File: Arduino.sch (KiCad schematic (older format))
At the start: 0 parts

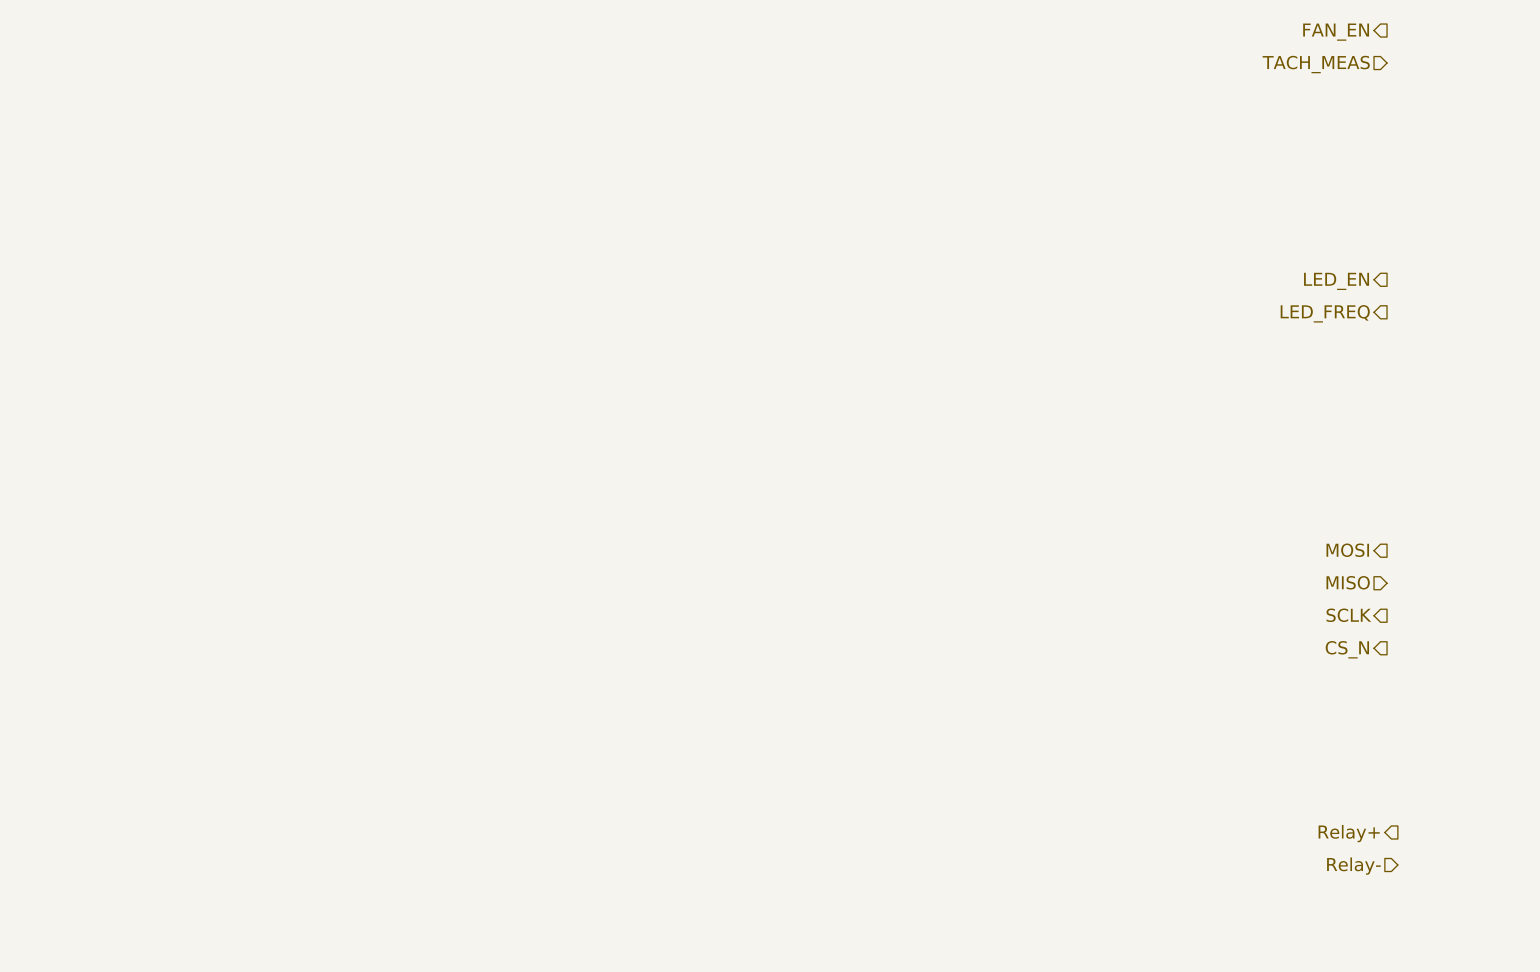
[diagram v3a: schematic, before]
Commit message: Completed Arduino Module Video
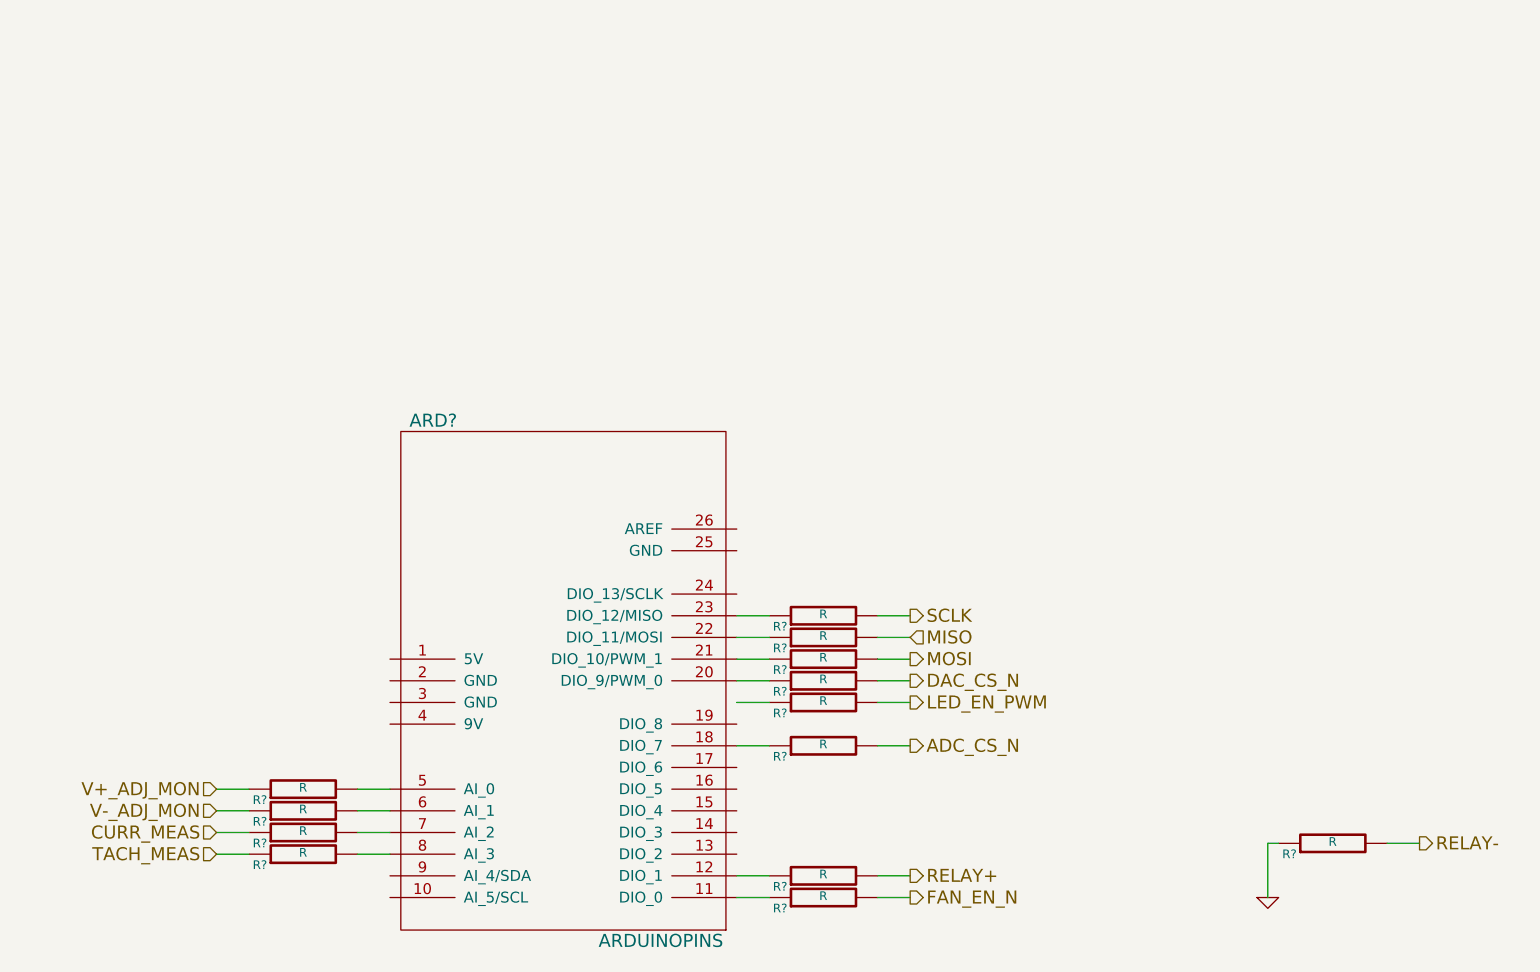
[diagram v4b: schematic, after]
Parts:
- added ARD?: ARDUINOPINS, symbol ARDUINOPINS
- added R? (x13): R, ~, symbol R
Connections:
- net MISO: now also R?.2
- net MOSI: now also R?.2
- net SCLK: now also R?.2
- net TACH_MEAS: now also R?.1
- new net: ARD?.11 (DIO_0), R?.1
- new net: ARD?.12 (DIO_1), R?.1
- new net: ARD?.18 (DIO_7), R?.1
- new net: ARD?.20 (DIO_9/PWM_0), R?.1
- new net: ARD?.21 (DIO_10/PWM_1), R?.1
- new net: ARD?.22 (DIO_11/MOSI), R?.1
- new net: ARD?.23 (DIO_12/MISO), R?.1
- new net: ARD?.5 (AI_0), R?.2
- new net: ARD?.6 (AI_1), R?.2
- new net: ARD?.7 (AI_2), R?.2
- new net: ARD?.8 (AI_3), R?.2
- new net ADC_CS_N: R?.2
- new net CURR_MEAS: R?.1
- new net DAC_CS_N: R?.2
- new net FAN_EN_N: R?.2
- new net GND: R?.1
- new net LED_EN_PWM: R?.2
- new net RELAY+: R?.2
- new net RELAY-: R?.2
- new net V+_ADJ_MON: R?.1
- new net V-_ADJ_MON: R?.1

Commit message: Fan Module Update
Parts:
- removed ARD?: ARDUINOPINS, symbol ARDUINOPINS
- added ARD?: ARDUINOPINS, ~, symbol ARDUINOPINS
- added R? (x2): R, ~, symbol R
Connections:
- net at R?.1: now also ARD?.20 (DIO_9/PWM_0)
- net at R?.1: now also ARD?.12 (DIO_1)
- net at R?.1: now also ARD?.18 (DIO_7)
- net at R?.1: now also ARD?.17 (DIO_6)
- net at R?.1: now also ARD?.21 (DIO_10/PWM_1)
- net at R?.1: now also ARD?.22 (DIO_11/MOSI)
- net at R?.1: now also ARD?.23 (DIO_12/MISO)
- net at R?.2: now also ARD?.5 (AI_0)
- net at R?.2: now also ARD?.6 (AI_1)
- net at R?.2: now also ARD?.7 (AI_2)
- net at R?.2: now also ARD?.8 (AI_3)
- net FAN_EN_N renamed FAN_PWM
- new net: ARD?.11 (DIO_0), R?.1
- new net: ARD?.4 (9V), R?.2
- new net +12P: R?.1
- new net FAN_MODE: R?.2
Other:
- moved on the sheet: R?
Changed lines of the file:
@@
 Text HLabel 6400 4100 2    60   Output ~ 0
 SCLK
+Text HLabel 6400 4800 2    60   Output ~ 0
+DAC_CS_N
 Text HLabel 6400 4400 2    60   Output ~ 0
-DAC_CS_N
-Text HLabel 6400 5400 2    60   Output ~ 0
-FAN_EN_N
+FAN_PWM
 Text HLabel 3200 5200 0    60   Input ~ 0
 TACH_MEAS
-$Comp
-L ARDUINOPINS ARD?
-U 1 1 52F9D8E3
-P 6350 4700
-F 0 "ARD?" H 4200 6200 60  0000 C CNN
-F 1 "ARDUINOPINS" H 5250 3800 60  0000 C CNN
-F 2 "" H 6350 4700 60  0000 C CNN
-F 3 "" H 6350 4700 60  0000 C CNN
-	1    6350 4700
-	1    0    0    -1
-$EndComp
 Text HLabel 3200 5100 0    60   Input ~ 0
 CURR_MEAS
@@
 L R R?
 U 1 1 52F9D91F
-P 6000 5400
-F 0 "R?" V 5950 5600 40  0000 C CNN
-F 1 "R" V 6007 5401 40  0000 C CNN
-F 2 "~" V 5930 5400 30  0000 C CNN
-F 3 "~" H 6000 5400 30  0000 C CNN
-	1    6000 5400
-	0    -1   -1   0
-$EndComp
-Wire Wire Line
-	5600 5400 5750 5400
-Wire Wire Line
-	6250 5400 6400 5400
+P 6000 4400
+F 0 "R?" V 5950 4600 40  0000 C CNN
+F 1 "R" V 6007 4401 40  0000 C CNN
+F 2 "~" V 5930 4400 30  0000 C CNN
+F 3 "~" H 6000 4400 30  0000 C CNN
+	1    6000 4400
+	0    -1   -1   0
+$EndComp
 $Comp
 L R R?
@@
 L R R?
 U 1 1 52FA6082
-P 6000 4400
-F 0 "R?" V 5950 4600 40  0000 C CNN
-F 1 "R" V 6007 4401 40  0000 C CNN
-F 2 "~" V 5930 4400 30  0000 C CNN
-F 3 "~" H 6000 4400 30  0000 C CNN
-	1    6000 4400
+P 6000 4800
+F 0 "R?" V 5950 5000 40  0000 C CNN
+F 1 "R" V 6007 4801 40  0000 C CNN
+F 2 "~" V 5930 4800 30  0000 C CNN
+F 3 "~" H 6000 4800 30  0000 C CNN
+	1    6000 4800
 	0    -1   -1   0
 $EndComp
@@
 $EndComp
 Wire Wire Line
-	6250 4400 6400 4400
-Wire Wire Line
 	6250 4300 6400 4300
 Wire Wire Line
@@
 Wire Wire Line
 	6250 4100 6400 4100
-Wire Wire Line
-	5750 4400 5600 4400
 Wire Wire Line
 	5750 4300 5600 4300
@@
 Wire Wire Line
 	6250 4700 6400 4700
+Wire Wire Line
+	5600 4800 5750 4800
+Wire Wire Line
+	6250 4800 6400 4800
+Wire Wire Line
+	6250 4400 6400 4400
+Wire Wire Line
+	5750 4400 5600 4400
+$Comp
+L ARDUINOPINS ARD?
+U 1 1 52FA4C31
+P 6350 4700
+F 0 "ARD?" H 4200 6200 60  0000 C CNN
+F 1 "ARDUINOPINS" H 5250 3800 60  0000 C CNN
+F 2 "~" H 6350 4700 60  0000 C CNN
+F 3 "~" H 6350 4700 60  0000 C CNN
+	1    6350 4700
+	1    0    0    -1
+$EndComp
+Text HLabel 6400 5400 2    60   Output ~ 0
+FAN_MODE
+$Comp
+L R R?
+U 1 1 52FA55B0
+P 6000 5400
+F 0 "R?" V 5950 5600 40  0000 C CNN
+F 1 "R" V 6007 5401 40  0000 C CNN
+F 2 "~" V 5930 5400 30  0000 C CNN
+F 3 "~" H 6000 5400 30  0000 C CNN
+	1    6000 5400
+	0    -1   -1   0
+$EndComp
+Wire Wire Line
+	5600 5400 5750 5400
+Wire Wire Line
+	6250 5400 6400 5400
+$Comp
+L R R?
+U 1 1 52FA5B06
+P 3600 4600
+F 0 "R?" V 3550 4800 40  0000 C CNN
+F 1 "R" V 3607 4601 40  0000 C CNN
+F 2 "~" V 3530 4600 30  0000 C CNN
+F 3 "~" H 3600 4600 30  0000 C CNN
+	1    3600 4600
+	0    -1   -1   0
+$EndComp
+Wire Wire Line
+	3850 4600 4000 4600
+$Comp
+L +12P #PWR?
+U 1 1 52FA5B4B
+P 2800 4500
+F 0 "#PWR?" H 2800 4470 30  0001 C CNN
+F 1 "+12P" H 2800 4600 30  0000 C CNN
+F 2 "" H 2800 4500 60  0000 C CNN
+F 3 "" H 2800 4500 60  0000 C CNN
+	1    2800 4500
+	1    0    0    -1
+$EndComp
+Wire Wire Line
+	2800 4500 2800 4600
+Wire Wire Line
+	2800 4600 3350 4600
 $EndSCHEMATC

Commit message: Started Layout Outline.  Completed other schem videos
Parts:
- removed ARD?: ARDUINOPINS, ~, symbol ARDUINOPINS
- added ARD?: ARDUINOPINS, ~, symbol ARDUINOPINS
- added R? (x3): R, ~, symbol R
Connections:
- net GND: now also R?.1, R?.1
- net at R?.1: now also ARD?.21 (DIO_10/PWM_1)
- net at R?.1: now also ARD?.12 (DIO_1)
- net at R?.2: now also ARD?.8 (AI_3)
- net at R?.2: now also ARD?.7 (AI_2)
- net at R?.1: now also ARD?.11 (DIO_0)
- net at R?.1: now also ARD?.18 (DIO_7)
- net at R?.1: now also ARD?.19 (DIO_8)
- net at R?.1: now also ARD?.22 (DIO_11/MOSI)
- net at R?.1: now also ARD?.23 (DIO_12/MISO)
- net at R?.1: now also ARD?.24 (DIO_13/SCLK)
- net at R?.2: now also ARD?.4 (9V)
- net at R?.2: now also ARD?.5 (AI_0)
- net at R?.2: now also ARD?.6 (AI_1)
- net at R?.1: now also ARD?.20 (DIO_9/PWM_0)
- new net: ARD?.1 (5V), R?.2
- new net: ARD?.2 (GND), R?.2
- new net: ARD?.3 (GND), R?.2
- new net +5V: R?.1
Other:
- moved on the sheet: R?
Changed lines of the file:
@@
 $Descr A4 11693 8268
 encoding utf-8
-Sheet 2 9
+Sheet 9 9
 Title ""
-Date "11 feb 2014"
+Date "17 feb 2014"
 Rev ""
 Comp ""
@@
 Text HLabel 8750 5150 2    60   Output ~ 0
 RELAY-
+Text HLabel 6400 4200 2    60   Output ~ 0
+MOSI
+Text HLabel 6400 4100 2    60   Input ~ 0
+MISO
+Text HLabel 6400 4000 2    60   Output ~ 0
+SCLK
+Text HLabel 6400 4700 2    60   Output ~ 0
+DAC_CS_N
 Text HLabel 6400 4300 2    60   Output ~ 0
-MOSI
-Text HLabel 6400 4200 2    60   Input ~ 0
-MISO
-Text HLabel 6400 4100 2    60   Output ~ 0
-SCLK
-Text HLabel 6400 4800 2    60   Output ~ 0
-DAC_CS_N
-Text HLabel 6400 4400 2    60   Output ~ 0
 FAN_PWM
 Text HLabel 3200 5200 0    60   Input ~ 0
@@
 L R R?
 U 1 1 52F9D91F
-P 6000 4400
-F 0 "R?" V 5950 4600 40  0000 C CNN
-F 1 "R" V 6007 4401 40  0000 C CNN
-F 2 "~" V 5930 4400 30  0000 C CNN
-F 3 "~" H 6000 4400 30  0000 C CNN
-	1    6000 4400
+P 6000 4300
+F 0 "R?" V 5950 4500 40  0000 C CNN
+F 1 "R" V 6007 4301 40  0000 C CNN
+F 2 "~" V 5930 4300 30  0000 C CNN
+F 3 "~" H 6000 4300 30  0000 C CNN
+	1    6000 4300
 	0    -1   -1   0
 $EndComp
@@
 L R R?
 U 1 1 52FA6082
-P 6000 4800
-F 0 "R?" V 5950 5000 40  0000 C CNN
-F 1 "R" V 6007 4801 40  0000 C CNN
-F 2 "~" V 5930 4800 30  0000 C CNN
-F 3 "~" H 6000 4800 30  0000 C CNN
-	1    6000 4800
+P 6000 4700
+F 0 "R?" V 5950 4900 40  0000 C CNN
+F 1 "R" V 6007 4701 40  0000 C CNN
+F 2 "~" V 5930 4700 30  0000 C CNN
+F 3 "~" H 6000 4700 30  0000 C CNN
+	1    6000 4700
 	0    -1   -1   0
 $EndComp
@@
 L R R?
 U 1 1 52FA6088
-P 6000 4300
-F 0 "R?" V 5950 4500 40  0000 C CNN
-F 1 "R" V 6007 4301 40  0000 C CNN
-F 2 "~" V 5930 4300 30  0000 C CNN
-F 3 "~" H 6000 4300 30  0000 C CNN
-	1    6000 4300
-	0    -1   -1   0
-$EndComp
-$Comp
-L R R?
-U 1 1 52FA608E
 P 6000 4200
 F 0 "R?" V 5950 4400 40  0000 C CNN
@@
 $Comp
 L R R?
-U 1 1 52FA6094
+U 1 1 52FA608E
 P 6000 4100
 F 0 "R?" V 5950 4300 40  0000 C CNN
@@
 	0    -1   -1   0
 $EndComp
+$Comp
+L R R?
+U 1 1 52FA6094
+P 6000 4000
+F 0 "R?" V 5950 4200 40  0000 C CNN
+F 1 "R" V 6007 4001 40  0000 C CNN
+F 2 "~" V 5930 4000 30  0000 C CNN
+F 3 "~" H 6000 4000 30  0000 C CNN
+	1    6000 4000
+	0    -1   -1   0
+$EndComp
+Wire Wire Line
+	6250 4200 6400 4200
+Wire Wire Line
+	6250 4100 6400 4100
+Wire Wire Line
+	6250 4000 6400 4000
+Wire Wire Line
+	5750 4200 5600 4200
+Wire Wire Line
+	5750 4100 5600 4100
+Wire Wire Line
+	5750 4000 5600 4000
+Text HLabel 6400 4400 2    60   Output ~ 0
+LED_EN_PWM
+$Comp
+L R R?
+U 1 1 52FA63A1
+P 6000 4400
+F 0 "R?" V 5950 4600 40  0000 C CNN
+F 1 "R" V 6007 4401 40  0000 C CNN
+F 2 "~" V 5930 4400 30  0000 C CNN
+F 3 "~" H 6000 4400 30  0000 C CNN
+	1    6000 4400
+	0    -1   -1   0
+$EndComp
+Wire Wire Line
+	5750 4400 5600 4400
+Wire Wire Line
+	6250 4400 6400 4400
+Text HLabel 6400 4600 2    60   Output ~ 0
+ADC_CS_N
+$Comp
+L R R?
+U 1 1 52FA944C
+P 6000 4600
+F 0 "R?" V 5950 4800 40  0000 C CNN
+F 1 "R" V 6007 4601 40  0000 C CNN
+F 2 "~" V 5930 4600 30  0000 C CNN
+F 3 "~" H 6000 4600 30  0000 C CNN
+	1    6000 4600
+	0    -1   -1   0
+$EndComp
+Wire Wire Line
+	5600 4600 5750 4600
+Wire Wire Line
+	6250 4600 6400 4600
+Wire Wire Line
+	5600 4700 5750 4700
+Wire Wire Line
+	6250 4700 6400 4700
 Wire Wire Line
 	6250 4300 6400 4300
 Wire Wire Line
-	6250 4200 6400 4200
-Wire Wire Line
-	6250 4100 6400 4100
-Wire Wire Line
 	5750 4300 5600 4300
-Wire Wire Line
-	5750 4200 5600 4200
-Wire Wire Line
-	5750 4100 5600 4100
-Text HLabel 6400 4500 2    60   Output ~ 0
-LED_EN_PWM
-$Comp
-L R R?
-U 1 1 52FA63A1
-P 6000 4500
-F 0 "R?" V 5950 4700 40  0000 C CNN
-F 1 "R" V 6007 4501 40  0000 C CNN
-F 2 "~" V 5930 4500 30  0000 C CNN
-F 3 "~" H 6000 4500 30  0000 C CNN
-	1    6000 4500
-	0    -1   -1   0
-$EndComp
-Wire Wire Line
-	5750 4500 5600 4500
-Wire Wire Line
-	6250 4500 6400 4500
-Text HLabel 6400 4700 2    60   Output ~ 0
-ADC_CS_N
-$Comp
-L R R?
-U 1 1 52FA944C
-P 6000 4700
-F 0 "R?" V 5950 4900 40  0000 C CNN
-F 1 "R" V 6007 4701 40  0000 C CNN
-F 2 "~" V 5930 4700 30  0000 C CNN
-F 3 "~" H 6000 4700 30  0000 C CNN
-	1    6000 4700
-	0    -1   -1   0
-$EndComp
-Wire Wire Line
-	5600 4700 5750 4700
-Wire Wire Line
-	6250 4700 6400 4700
-Wire Wire Line
-	5600 4800 5750 4800
-Wire Wire Line
-	6250 4800 6400 4800
-Wire Wire Line
-	6250 4400 6400 4400
-Wire Wire Line
-	5750 4400 5600 4400
-$Comp
-L ARDUINOPINS ARD?
-U 1 1 52FA4C31
-P 6350 4700
-F 0 "ARD?" H 4200 6200 60  0000 C CNN
-F 1 "ARDUINOPINS" H 5250 3800 60  0000 C CNN
-F 2 "~" H 6350 4700 60  0000 C CNN
-F 3 "~" H 6350 4700 60  0000 C CNN
-	1    6350 4700
-	1    0    0    -1
-$EndComp
 Text HLabel 6400 5400 2    60   Output ~ 0
 FAN_MODE
@@
 L +12P #PWR?
 U 1 1 52FA5B4B
-P 2800 4500
-F 0 "#PWR?" H 2800 4470 30  0001 C CNN
-F 1 "+12P" H 2800 4600 30  0000 C CNN
-F 2 "" H 2800 4500 60  0000 C CNN
-F 3 "" H 2800 4500 60  0000 C CNN
-	1    2800 4500
-	1    0    0    -1
-$EndComp
-Wire Wire Line
-	2800 4500 2800 4600
-Wire Wire Line
-	2800 4600 3350 4600
+P 2350 4500
+F 0 "#PWR?" H 2350 4470 30  0001 C CNN
+F 1 "+12P" H 2350 4600 30  0000 C CNN
+F 2 "" H 2350 4500 60  0000 C CNN
+F 3 "" H 2350 4500 60  0000 C CNN
+	1    2350 4500
+	1    0    0    -1
+$EndComp
+Wire Wire Line
+	2350 4500 2350 4650
+$Comp
+L ARDUINOPINS ARD?
+U 1 1 53022634
+P 6350 4700
+F 0 "ARD?" H 4200 6200 60  0000 C CNN
+F 1 "ARDUINOPINS" H 5250 3800 60  0000 C CNN
+F 2 "~" H 6350 4700 60  0000 C CNN
+F 3 "~" H 6350 4700 60  0000 C CNN
+	1    6350 4700
+	1    0    0    -1
+$EndComp
+$Comp
+L R R?
+U 1 1 53023A69
+P 3600 4300
+F 0 "R?" V 3550 4500 40  0000 C CNN
+F 1 "R" V 3607 4301 40  0000 C CNN
+F 2 "~" V 3530 4300 30  0000 C CNN
+F 3 "~" H 3600 4300 30  0000 C CNN
+	1    3600 4300
+	0    -1   -1   0
+$EndComp
+$Comp
+L R R?
+U 1 1 53023A6F
+P 3600 4400
+F 0 "R?" V 3550 4600 40  0000 C CNN
+F 1 "R" V 3607 4401 40  0000 C CNN
+F 2 "~" V 3530 4400 30  0000 C CNN
+F 3 "~" H 3600 4400 30  0000 C CNN
+	1    3600 4400
+	0    -1   -1   0
+$EndComp
+$Comp
+L R R?
+U 1 1 53023A7F
+P 3600 4500
+F 0 "R?" V 3550 4700 40  0000 C CNN
+F 1 "R" V 3607 4501 40  0000 C CNN
+F 2 "~" V 3530 4500 30  0000 C CNN
+F 3 "~" H 3600 4500 30  0000 C CNN
+	1    3600 4500
+	0    -1   -1   0
+$EndComp
+Wire Wire Line
+	3850 4500 4000 4500
+Wire Wire Line
+	3850 4400 4000 4400
+Wire Wire Line
+	3850 4300 4000 4300
+$Comp
+L +5V #PWR?
+U 1 1 53023B11
+P 2350 4200
+F 0 "#PWR?" H 2350 4290 20  0001 C CNN
+F 1 "+5V" H 2350 4290 30  0000 C CNN
+F 2 "" H 2350 4200 60  0000 C CNN
+F 3 "" H 2350 4200 60  0000 C CNN
+	1    2350 4200
+	1    0    0    -1
+$EndComp
+Wire Wire Line
+	2350 4200 2350 4300
+Wire Wire Line
+	2350 4300 3350 4300
+$Comp
+L GND #PWR?
+U 1 1 53023B7D
+P 2600 4550
+F 0 "#PWR?" H 2600 4550 30  0001 C CNN
+F 1 "GND" H 2600 4480 30  0001 C CNN
+F 2 "" H 2600 4550 60  0000 C CNN
+F 3 "" H 2600 4550 60  0000 C CNN
+	1    2600 4550
+	1    0    0    -1
+$EndComp
+Wire Wire Line
+	2600 4400 2600 4550
+Wire Wire Line
+	2600 4500 3350 4500
+Wire Wire Line
+	3350 4400 2600 4400
+Connection ~ 2600 4500
+Wire Wire Line
+	3350 4600 2750 4600
+Wire Wire Line
+	2750 4600 2750 4650
+Wire Wire Line
+	2750 4650 2350 4650
 $EndSCHEMATC
